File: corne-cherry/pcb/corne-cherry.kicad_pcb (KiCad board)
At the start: 2 copper layers, 295.5 x 105.6 mm, 206 parts, among them J1 CONN_DISPLAY_SOCKET, J1 MJ-4PP-9, J2 Conn_01x02, J2 OLED, J3 MJ-4PP-9, J4 CONN_DISPLAY_SOCKET, J4 OLED, J5 Conn_01x02, SW1 SW_PUSH, SW10 SW_PUSH, SW11 SW_PUSH, SW12 SW_PUSH, SW13 SW_PUSH, SW14 SW_PUSH, SW15 SW_PUSH, SW16 SW_PUSH, SW17 SW_PUSH, SW18 SW_PUSH, SW19 SW_PUSH, SW2 SW_PUSH, SW20 SW_PUSH, SW21 SW_PUSH, SW22 SW_PUSH, SW23 SW_PUSH, SW24 SW_PUSH, SW25 SW_PUSH, SW26 SW_PUSH, SW27 SW_PUSH, SW28 SW_PUSH, SW29 SW_PUSH, SW3 SW_PUSH, SW30 SW_PUSH, SW31 SW_PUSH, SW32 SW_PUSH, SW33 SW_PUSH, SW34 SW_PUSH, SW35 SW_PUSH, SW36 SW_PUSH, SW37 SW_PUSH, SW38 SW_PUSH, SW39 SW_PUSH, SW4 SW_PUSH, SW40 SW_PUSH, SW41 SW_PUSH, SW42 SW_PUSH, SW43 SW_RGB_UNDERGLOW, SW44 SW_RGB_PERKEY, SW45 SW_RGB_LED_OLED, SW46 SW_RGB_PERKEY, SW47 SW_RGB_PERKEY, SW48 SW_RGB_LED_OLED, SW49 SW_RGB_UNDERGLOW, SW5 SW_PUSH, SW50 SW_RGB_PERKEY, SW6 SW_PUSH, SW7 SW_PUSH, SW8 SW_PUSH, SW9 SW_PUSH, U1 ProMicro, U1 xiao-ble, U2 ProMicro, U2 xiao-ble

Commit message: finished track routing.
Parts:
- removed the D1 at (27.7, 35.8)
- removed the D22 at (284.2, 35.8)
- removed the G*** at (58.3, 80.9)
- removed the G*** at (238.8, 81.0)
- removed the G*** at (58.0, 80.9)
- removed the G*** at (238.6, 81.0)
- removed the J1 at (144.1, 74.3)
- removed the J2 at (130.9, 67.0)
- removed the J4 at (158.2, 67.0)
- removed LED19, LED46: YS-SK6812MINI-E, kbd:YS-SK6812MINI-E
- removed the REF** at (58.2, 21.9)
- removed the REF** at (96.2, 21.9)
- removed the REF** at (20.2, 83.2)
- removed the REF** at (58.1, 83.2)
- removed the REF** at (276.7, 83.2)
- removed the REF** at (200.7, 21.9)
- removed the REF** at (238.6, 21.9)
- removed the REF** at (238.7, 83.2)
- removed RSW1, RSW2: SW_PUSH, kbd:ResetSW_1side
- removed the Ref** at (168.9, 74.3)
- removed SW1, SW22: SW_PUSH, kbd:CherryMX_Hotswap
- removed SW43, SW49: SW_RGB_UNDERGLOW, Button_Switch_SMD:SW_SPDT_CK-JS102011SAQN
- removed SW44, SW50: SW_RGB_PERKEY, Button_Switch_SMD:SW_SPDT_CK-JS102011SAQN
- removed SW45, SW48: SW_RGB_LED_OLED, Button_Switch_SMD:SW_SPDT_CK-JS102011SAQN
- removed U1, U2: ProMicro, kbd:ProMicro_v3
- added G***: LOGO, keyboard:corne-logo-horizontal_F.CU, F.Cu at (237.6, 81.0)
- added G***: LOGO, keyboard:corne-logo-horizontal_F.CU, F.Cu at (58.6, 80.9)
- added G***: LOGO, keyboard:corne-logo-horizontal-B.CU, F.Cu at (58.7, 80.9)
- added G***: LOGO, keyboard:corne-logo-horizontal-B.CU, F.Cu at (237.8, 81.1)
- added J6: Conn_01x01_Socket, Jumper:SolderJumper-2_P1.3mm_Bridged_RoundedPad1.0x1.5mm, B.Cu at (156.2, 54.0)
- added J7: Conn_01x01_Socket, Jumper:SolderJumper-2_P1.3mm_Bridged_RoundedPad1.0x1.5mm, B.Cu at (141.0, 54.0)
- added J8: Conn_01x01_Socket, Jumper:SolderJumper-2_P1.3mm_Bridged_RoundedPad1.0x1.5mm, B.Cu at (158.8, 54.0)
- added JP1: SolderJumper, Jumper:SolderJumper-3_P1.3mm_Open_Pad1.0x1.5mm_NumberLabels, B.Cu at (134.6, 52.1)
- added JP2: SolderJumper, Jumper:SolderJumper-3_P1.3mm_Open_Pad1.0x1.5mm_NumberLabels, B.Cu at (163.8, 52.5)
- added OFF ON: SW_ONOFF, Button_Switch_SMD:SW_SPDT_PCM12, F.Cu at (142.9, 74.9)
- added ON OFF: SW_ONOFF_R, Button_Switch_SMD:SW_SPDT_PCM12, F.Cu at (154.0, 74.7)
- added REF**: Breakaway_Tabs, foolstan_kbd:Breakaway_Tabs, F.Cu at (145.1, 82.5)
- added REF**: Breakaway_Tabs, foolstan_kbd:Breakaway_Tabs, F.Cu at (151.8, 33.0)
- added REF**: Breakaway_Tabs, foolstan_kbd:Breakaway_Tabs, F.Cu at (145.1, 33.1)
- added REF**: Breakaway_Tabs, foolstan_kbd:Breakaway_Tabs, F.Cu at (151.8, 82.6)
- BLE: renamed from U2; footprint Seeed Studio XIAO Series Library:XIAO-nRF52840-Sense-14P-2.54-21X17.8MM -> Seeed Studio XIAO Series Library:XIAO-Generic-Thruhole-14P-2.54-21X17.8MM
- BLE: renamed from U1; footprint Seeed Studio XIAO Series Library:XIAO-nRF52840-Sense-14P-2.54-21X17.8MM -> Seeed Studio XIAO Series Library:XIAO-Generic-Thruhole-14P-2.54-21X17.8MM
- D1, D22, D43, D44, D45, D46, D47, D48, D49, D50, R1, R10, R2, R3, R4, R5, R6, R7, R8, R9: moved to B.Cu
- D7: footprint kbd:D3_SMD_v2 -> foolstan_kbd:D3_SMD_v2
- J1, J4: footprint Connector_PinSocket_1.27mm:PinSocket_1x05_P1.27mm_Vertical -> Connector_PinSocket_2.54mm:PinSocket_1x05_P2.54mm_Vertical
- J2: footprint Connector_AMASS:AMASS_XT30PW-F_1x02_P2.50mm_Horizontal -> Connector_JST:JST_PH_S2B-PH-K_1x02_P2.00mm_Horizontal; moved to B.Cu
- J3: value MJ-4PP-9 -> Conn_01x02; footprint kbd:MJ-4PP-9_1side -> Connector_JST:JST_PH_S2B-PH-K_1x02_P2.00mm_Horizontal; moved to B.Cu
- J5: value Conn_01x02 -> Conn_01x01_Socket; footprint Connector_AMASS:AMASS_XT30PW-F_1x02_P2.50mm_Horizontal -> Jumper:SolderJumper-2_P1.3mm_Bridged_RoundedPad1.0x1.5mm; moved to B.Cu
- LED SW: renamed from SW47; value SW_RGB_PERKEY -> SW_LED_PERM; footprint Button_Switch_SMD:SW_SPDT_CK-JS102011SAQN -> Button_Switch_SMD:SW_SPDT_PCM12
- LED SW: renamed from SW46; value SW_RGB_PERKEY -> SW_LED_PERM; footprint Button_Switch_SMD:SW_SPDT_CK-JS102011SAQN -> Button_Switch_SMD:SW_SPDT_PCM12
- moved D48 194.6 mm to (281.9, 53.3), turned to 180 degrees
- moved R8 182.3 mm to (275.1, 53.3), turned to 180 degrees
- moved R9 175.1 mm to (246.7, 24.2), turned to -90 degrees
- moved D49 174.7 mm to (238.8, 23.4)
- moved D47 153.8 mm to (120.7, 25.4), turned to 180 degrees
- moved LED SW 146.0 mm to (142.8, 61.1), turned to 90 degrees
- moved R5 145.2 mm to (113.5, 25.4), turned to 180 degrees
- moved J1 138.5 mm to (130.6, 67.4), turned to 90 degrees
- moved D22 132.5 mm to (227.9, 82.5), turned to -90 degrees
- moved D50 132.2 mm to (174.8, 25.4)
- moved R10 131.0 mm to (179.1, 25.4)
- moved R7 122.7 mm to (225.2, 85.4), turned to 180 degrees
- moved BLE 121.9 mm to (134.4, 38.2)
- moved R4 120.8 mm to (65.6, 22.9)
- moved D46 119.1 mm to (57.6, 23.5)
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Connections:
- J5 pad 1: Net-(J5-Pin_1) -> Net-(J2-Pin_2)
- J5 pad 2: Net-(J5-Pin_2) -> (no net)
- LED SW pad 1: unconnected-(SW47-A-Pad1) -> VCC_LED_R_PERM
- LED SW pad 3: VCC_LED_R_PERM -> unconnected-(SW47-C-Pad3)
- LED SW pad 1: unconnected-(SW46-A-Pad1) -> VCC_LED_PERM
- LED SW pad 3: VCC_LED_PERM -> unconnected-(SW46-C-Pad3)
- LED1 pad 1: VCC_LED_UNDERGLOW -> VCC
- LED10 pad 1: VCC_LED_PERKEY -> VCC
- LED11 pad 1: VCC_LED_PERKEY -> VCC
- LED12 pad 1: VCC_LED_PERKEY -> VCC
- LED13 pad 1: VCC_LED_PERKEY -> VCC
- LED14 pad 1: VCC_LED_PERKEY -> VCC
- LED15 pad 1: VCC_LED_PERKEY -> VCC
- LED16 pad 1: VCC_LED_PERKEY -> VCC
- LED17 pad 1: VCC_LED_PERKEY -> VCC
- LED18 pad 1: VCC_LED_PERKEY -> VCC
- LED2 pad 1: VCC_LED_UNDERGLOW -> VCC
- LED20 pad 1: VCC_LED_PERKEY -> VCC
- LED21 pad 1: VCC_LED_PERKEY -> VCC
- LED22 pad 1: VCC_LED_PERKEY -> VCC
- LED23 pad 1: VCC_LED_PERKEY -> VCC
- LED24 pad 1: VCC_LED_PERKEY -> VCC
- LED25 pad 1: VCC_LED_PERKEY -> VCC
- LED26 pad 1: VCC_LED_PERKEY -> VCC
- LED27 pad 1: VCC_LED_PERKEY -> VCC
- LED28 pad 1: VCC_LED_R_UNDERGLOW -> VDD
- LED29 pad 1: VCC_LED_R_UNDERGLOW -> VDD
- LED3 pad 1: VCC_LED_UNDERGLOW -> VCC
- LED30 pad 1: VCC_LED_R_UNDERGLOW -> VDD
- LED31 pad 1: VCC_LED_R_UNDERGLOW -> VDD
- LED31 pad 2: Net-(LED28-DOUT) -> Net-(LED31-DOUT)
- LED32 pad 1: VCC_LED_R_UNDERGLOW -> VDD
- LED32 pad 2: Net-(LED28-DOUT) -> Net-(LED32-DOUT)
- LED32 pad 4: Net-(LED28-DOUT) -> Net-(LED31-DOUT)
- LED33 pad 1: VCC_LED_R_UNDERGLOW -> VDD
- LED33 pad 2: Net-(LED28-DOUT) -> Net-(LED33-DOUT)
- LED33 pad 4: Net-(LED28-DOUT) -> Net-(LED32-DOUT)
- LED34 pad 1: VCC_LED_R_PERKEY -> VDD
- LED35 pad 1: VCC_LED_R_PERKEY -> VDD
- LED36 pad 1: VCC_LED_R_PERKEY -> VDD
- LED37 pad 1: VCC_LED_R_PERKEY -> VDD
- LED38 pad 1: VCC_LED_R_PERKEY -> VDD
- LED39 pad 1: VCC_LED_R_PERKEY -> VDD
- LED4 pad 1: VCC_LED_UNDERGLOW -> VCC
- LED40 pad 1: VCC_LED_R_PERKEY -> VDD
- LED41 pad 1: VCC_LED_R_PERKEY -> VDD
- LED42 pad 1: VCC_LED_R_PERKEY -> VDD
- LED43 pad 1: VCC_LED_R_PERKEY -> VDD
- LED44 pad 1: VCC_LED_R_PERKEY -> VDD
- LED45 pad 1: VCC_LED_R_PERKEY -> VDD
- LED47 pad 1: VCC_LED_R_PERKEY -> VDD
- LED48 pad 1: VCC_LED_R_PERKEY -> VDD
- LED49 pad 1: VCC_LED_R_PERKEY -> VDD
- LED5 pad 1: VCC_LED_UNDERGLOW -> VCC
- LED50 pad 1: VCC_LED_R_PERKEY -> VDD
- LED51 pad 1: VCC_LED_R_PERKEY -> VDD
- LED52 pad 1: VCC_LED_R_PERKEY -> VDD
- LED53 pad 1: VCC_LED_R_PERKEY -> VDD
- LED54 pad 1: VCC_LED_R_PERKEY -> VDD
- LED54 pad 4: Net-(LED28-DOUT) -> Net-(LED33-DOUT)
- LED6 pad 1: VCC_LED_UNDERGLOW -> VCC
- LED7 pad 1: VCC_LED_PERKEY -> VCC
- LED8 pad 1: VCC_LED_PERKEY -> VCC
- LED9 pad 1: VCC_LED_PERKEY -> VCC
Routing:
- net VCC_LED_R_PERM: track 0.00 -> 297.4 mm, vias 0 -> 23
- net VCC_LED_PERM: track 0.00 -> 287.8 mm, vias 0 -> 14
- net col0_r: track 175.8 -> 0.00 mm
- net col0: track 170.3 -> 0.00 mm
- net Net-(LED28-DOUT): track 193.6 -> 26.7 mm, vias 6 -> 2
- net row3_r: track 95.3 -> 236.3 mm, vias 2 -> 9
- net col2: track 125.8 -> 219.2 mm, vias 10 -> 9
- net reset_r: track 85.4 -> 0.00 mm
- net row3: track 121.7 -> 199.5 mm, vias 2 -> 4
- net data: track 77.0 -> 0.00 mm
- net Net-(LED31-DOUT): track 0.00 -> 71.8 mm, vias 0 -> 2
- net data_r: track 62.9 -> 0.00 mm
- net row0: track 183.2 -> 123.1 mm, vias 2 -> 4
- net reset: track 60.0 -> 0.00 mm
- net row1: track 193.3 -> 143.8 mm, vias 2 -> 1
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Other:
- board size 295.5 x 105.6 mm -> 274.6 x 91.4 mm
- board text added: "+"
- board text removed: "Corne Cherry v3.0.1 PCB Designed by foostan"

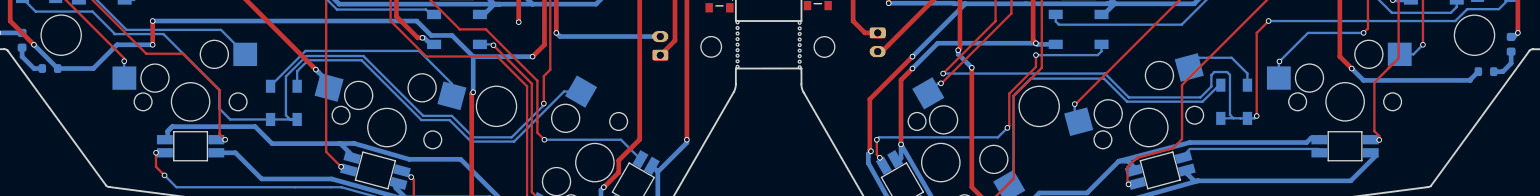
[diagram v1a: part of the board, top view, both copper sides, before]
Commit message: corne-cherry.kicad_pcb: fixed some DRCs and rerouted some tracks.
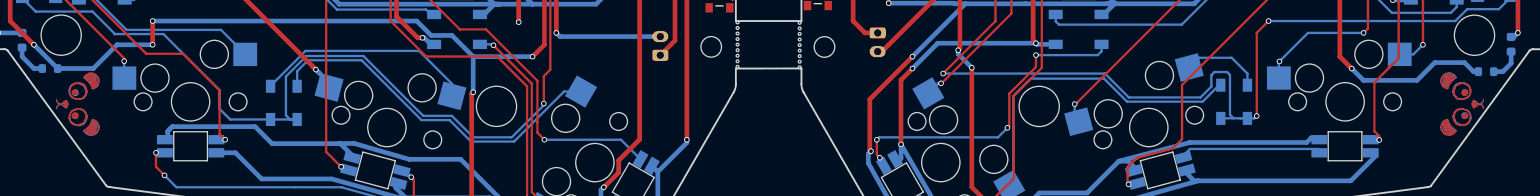
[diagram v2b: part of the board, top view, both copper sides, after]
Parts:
- added G***: LOGO, Panda-Logo:Panda_Logo_07mm, F.Cu at (74.3, 88.9)
- added G***: LOGO, Panda-Logo:Panda_Logo_07mm, F.Cu at (222.9, 88.9)
- added G***: LOGO, Panda-Logo:Panda_Logo_07mm, B.Cu at (222.9, 88.9)
- added G***: LOGO, Panda-Logo:Panda_Logo_07mm, B.Cu at (74.3, 88.9)
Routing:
- net VCC_LED_R_PERM: track 297.4 -> 298.1 mm
